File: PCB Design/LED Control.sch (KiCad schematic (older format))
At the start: 19 parts, among them J1 TO WS2812B LED STRIP, SW1 SW_Push_Dual

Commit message: circuit schematic complete
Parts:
- removed C1: 10uF, symbol Device:CP
- removed C1: 0.1nF, symbol Device:C
- added C1, C?: 0.1uF, symbol Device:C_Small
- added C?: C_Small, symbol Device:C_Small
- added C?: C, symbol Device:C
- added J?: Conn_01x03, symbol Connector_Generic:Conn_01x03
- added R?: R, symbol Device:R
- A1: symbol MCU_Module:Arduino_Nano_v3.x -> LED-Control-rescue:Arduino_Nano_v3.x-MCU_Module
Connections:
- net labels added: A3, DATA_IN, SS_DATA_OUT, SS_GND, SS_PWR, WS_GND, WS_PWR
- net labels removed: 5V_PWR, DATA, Earth
- wire segments 67 -> 93
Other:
- note added: "MICROCONTROLLER"
- note added: "POWER LINES"
- note added: "SOUND SENSOR"
- moved on the sheet: D1, D2, D3, J1, R1, R2, R3, R4, R5, R6, RV1, RV2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

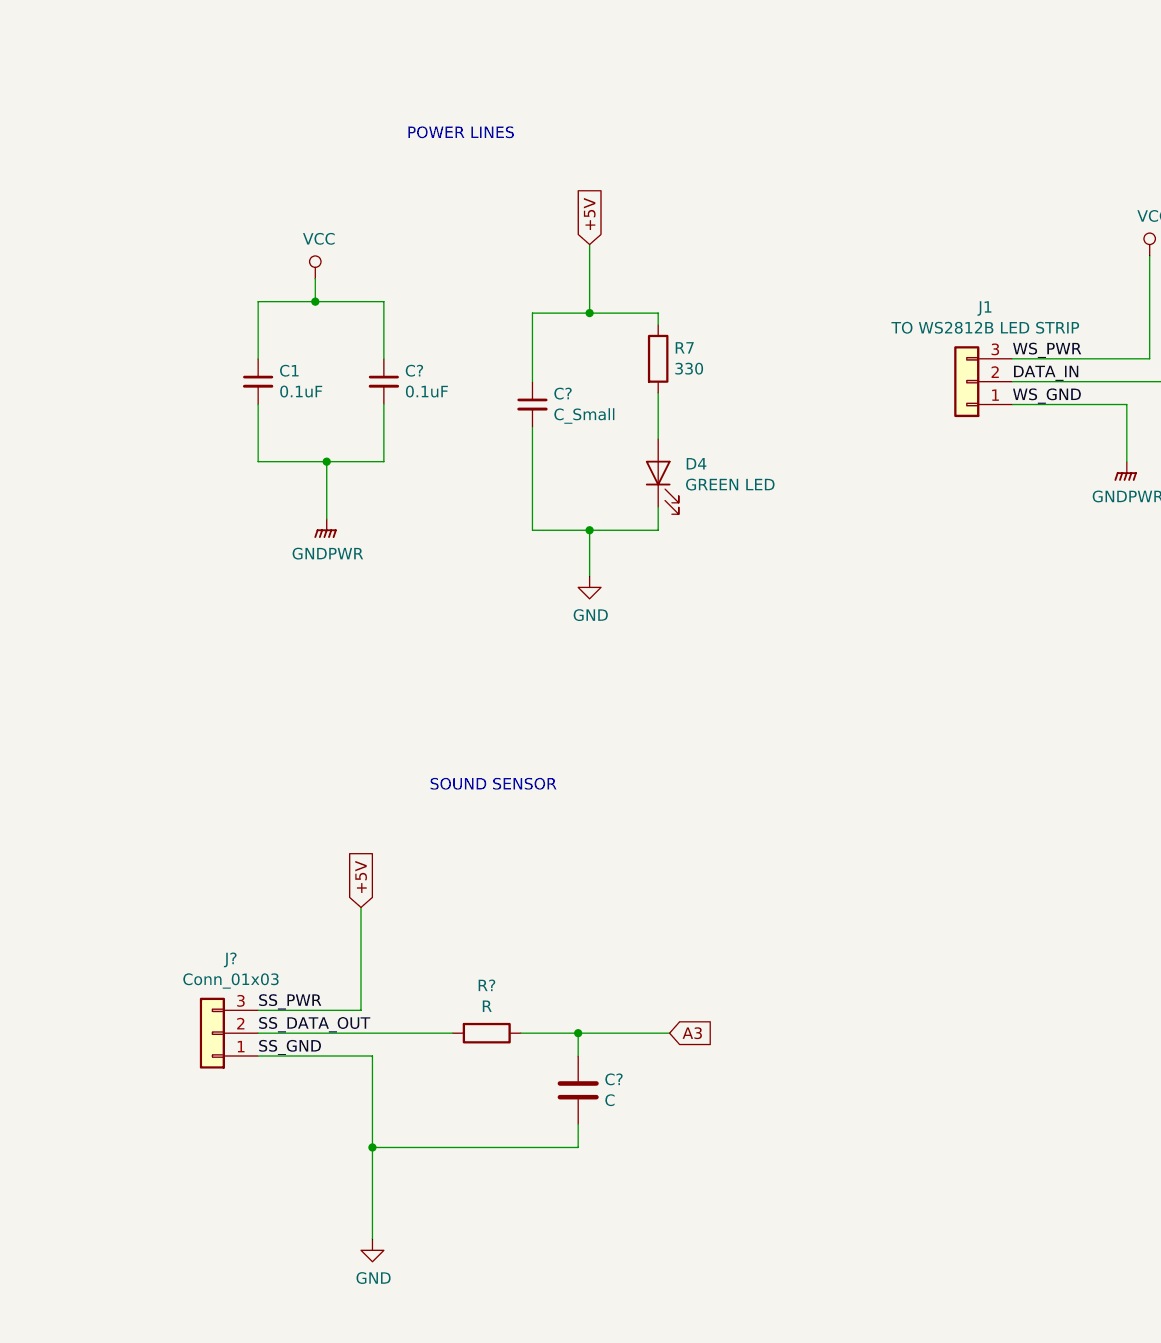
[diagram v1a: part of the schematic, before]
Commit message: PCB footprints added
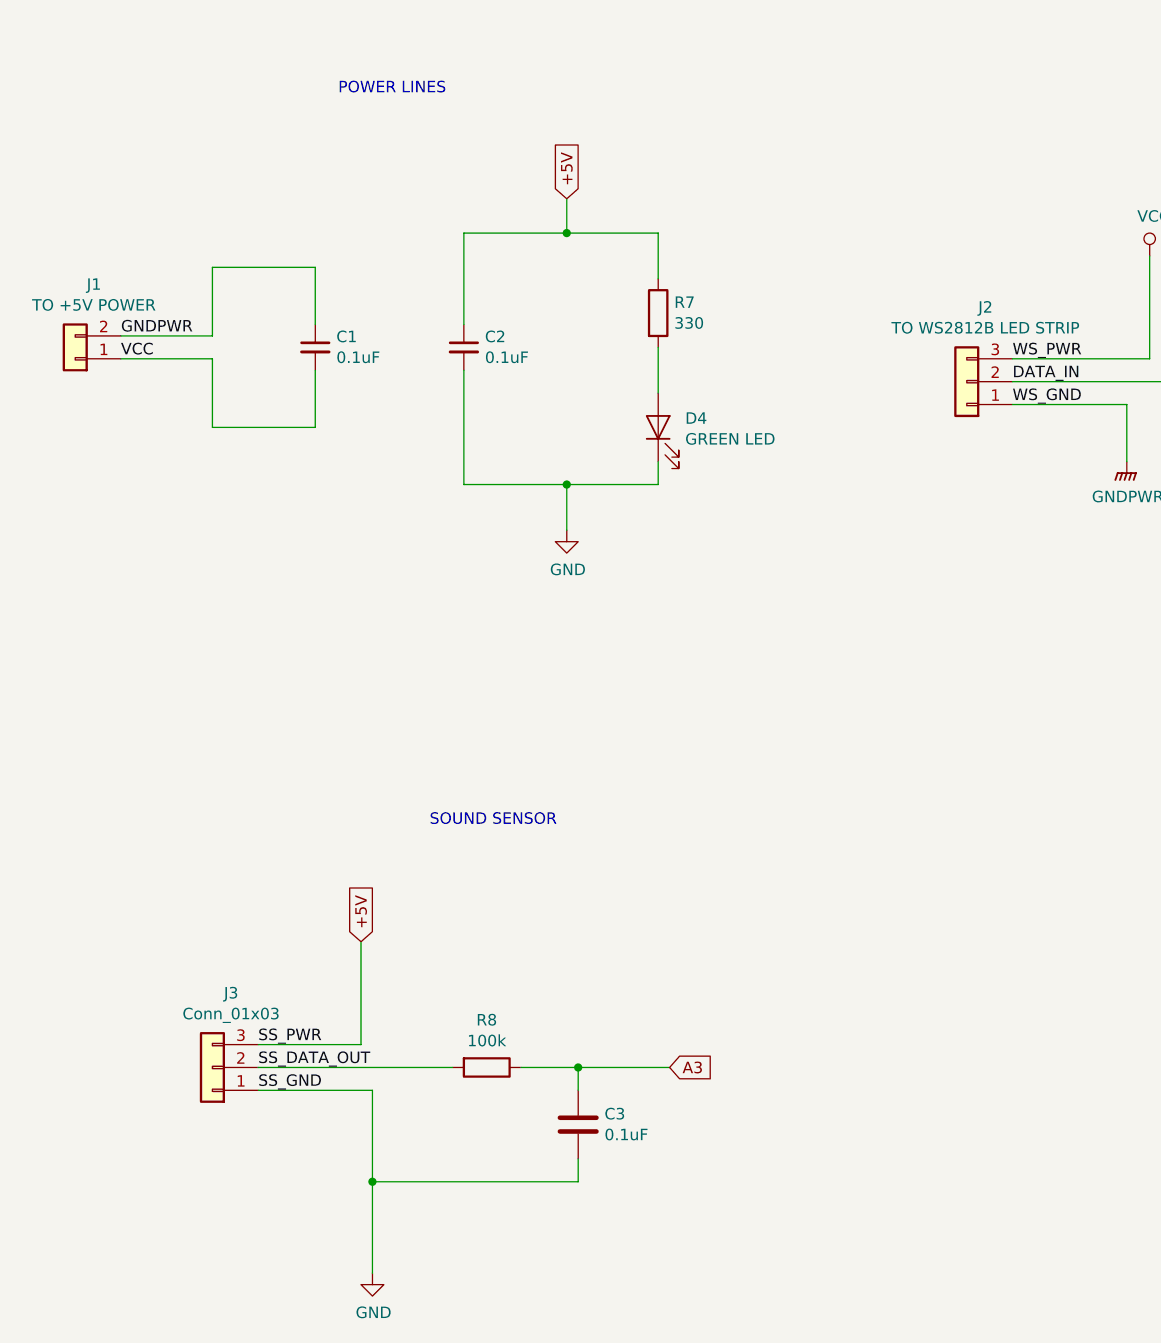
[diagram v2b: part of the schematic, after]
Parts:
- removed C?: C_Small, symbol Device:C_Small
- added J1: TO +5V POWER, TerminalBlock_Phoenix:TerminalBlock_Phoenix_PT-1,5-2-3.5-H_1x02_P3.50mm_Horizontal, symbol Connector_Generic:Conn_01x02
- C1: footprint (none) -> Capacitor_THT:C_Disc_D3.0mm_W1.6mm_P2.50mm
- C2: renamed from C?; footprint (none) -> Capacitor_THT:C_Disc_D3.0mm_W1.6mm_P2.50mm
- C3: renamed from C?; value C -> 0.1uF; footprint (none) -> Capacitor_THT:C_Disc_D3.0mm_W2.0mm_P2.50mm
- D1, D2, D3, D4: footprint (none) -> LED_THT:LED_D5.0mm
- J2: renamed from J1; footprint (none) -> TerminalBlock_Phoenix:TerminalBlock_Phoenix_MPT-0,5-3-2.54_1x03_P2.54mm_Horizontal
- J3: renamed from J?; footprint (none) -> TerminalBlock_Phoenix:TerminalBlock_Phoenix_MPT-0,5-3-2.54_1x03_P2.54mm_Horizontal
- R1, R2, R3, R4, R5, R6, R7: footprint (none) -> Resistor_THT:R_Axial_DIN0207_L6.3mm_D2.5mm_P10.16mm_Horizontal
- R8: renamed from R?; value R -> 100k; footprint (none) -> Resistor_THT:R_Axial_DIN0207_L6.3mm_D2.5mm_P10.16mm_Horizontal
- RV1, RV2, RV3: footprint (none) -> Custom Footprint:Potentiometer_4mm_Pitch
- SW1: footprint (none) -> Button_Switch_THT:SW_PUSH_6mm_H13mm
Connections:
- net +5V: now also C2.1
- net GND: now also C2.2
- net GNDPWR: now also C1.1, J1.2 (Pin_2); no longer C1.2, C2.2
- net VCC: now also C1.2, J1.1 (Pin_1); no longer C1.1, C2.1
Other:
- moved on the sheet: C1, C2, C3, D4, J3, R7, R8

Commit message: connectors selected and footprints updated
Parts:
- removed C3: 0.1uF, Capacitor_THT:C_Disc_D3.0mm_W2.0mm_P2.50mm, symbol Device:C
- removed J1: TO +5V POWER, TerminalBlock_Phoenix:TerminalBlock_Phoenix_PT-1,5-2-3.5-H_1x02_P3.50mm_Horizontal, symbol Connector_Generic:Conn_01x02
- added C2, C5: 0.1uF, Capacitor_THT:C_Disc_D3.0mm_W1.6mm_P2.50mm, symbol Device:C_Small
- added C4: 1uF, Capacitor_THT:C_Disc_D3.0mm_W1.6mm_P2.50mm, symbol Device:C_Small
- added J1: 5V 5A Power, PJ-002AH:CUI_PJ-002AH, symbol Connector:Barrel_Jack_Switch
- J2: footprint TerminalBlock_Phoenix:TerminalBlock_Phoenix_MPT-0,5-3-2.54_1x03_P2.54mm_Horizontal -> Connector_JST:JST_PH_S3B-PH-K_1x03_P2.00mm_Horizontal
- renumbered C2 to C3
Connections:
- net +5V: now also C4.1
- net A3: now also C5.1
- net GND: now also C4.2, C5.2
- net GNDPWR: now also C1.2, J2.3 (Pin_3), C2.2, J1.2; no longer C1.1, J2.1 (Pin_1)
- net VCC: now also C1.1, J2.1 (Pin_1), C2.1, J1.1; no longer C1.2, J2.3 (Pin_3)
- no-connect marks 2 -> 22
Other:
- moved on the sheet: A1, C1, C3, D1, D2, D3, D4, J2, J3, R1, R2, R3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

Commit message: capacitor footprints changed to axial
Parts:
- C1, C2, C3, C4, C5: footprint Capacitor_THT:C_Disc_D3.0mm_W1.6mm_P2.50mm -> Capacitor_THT:C_Axial_L3.8mm_D2.6mm_P7.50mm_Horizontal
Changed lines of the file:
@@
 F 0 "C1" H 3142 1996 50  0000 L CNN
 F 1 "0.1uF" H 3142 1905 50  0000 L CNN
-F 2 "Capacitor_THT:C_Disc_D3.0mm_W1.6mm_P2.50mm" H 3050 1950 50  0001 C CNN
+F 2 "Capacitor_THT:C_Axial_L3.8mm_D2.6mm_P7.50mm_Horizontal" H 3050 1950 50  0001 C CNN
 F 3 "~" H 3050 1950 50  0001 C CNN
 	1    3050 1950
@@
 F 0 "C3" H 2242 3646 50  0000 L CNN
 F 1 "0.1uF" H 2242 3555 50  0000 L CNN
-F 2 "Capacitor_THT:C_Disc_D3.0mm_W1.6mm_P2.50mm" H 2150 3600 50  0001 C CNN
+F 2 "Capacitor_THT:C_Axial_L3.8mm_D2.6mm_P7.50mm_Horizontal" H 2150 3600 50  0001 C CNN
 F 3 "~" H 2150 3600 50  0001 C CNN
 	1    2150 3600
@@
 F 0 "C2" H 3592 1996 50  0000 L CNN
 F 1 "0.1uF" H 3592 1905 50  0000 L CNN
-F 2 "Capacitor_THT:C_Disc_D3.0mm_W1.6mm_P2.50mm" H 3500 1950 50  0001 C CNN
+F 2 "Capacitor_THT:C_Axial_L3.8mm_D2.6mm_P7.50mm_Horizontal" H 3500 1950 50  0001 C CNN
 F 3 "~" H 3500 1950 50  0001 C CNN
 	1    3500 1950
@@
 F 0 "C4" H 2792 3646 50  0000 L CNN
 F 1 "1uF" H 2792 3555 50  0000 L CNN
-F 2 "Capacitor_THT:C_Disc_D3.0mm_W1.6mm_P2.50mm" H 2700 3600 50  0001 C CNN
+F 2 "Capacitor_THT:C_Axial_L3.8mm_D2.6mm_P7.50mm_Horizontal" H 2700 3600 50  0001 C CNN
 F 3 "~" H 2700 3600 50  0001 C CNN
 	1    2700 3600
@@
 F 0 "C5" H 3642 6496 50  0000 L CNN
 F 1 "0.1uF" H 3642 6405 50  0000 L CNN
-F 2 "Capacitor_THT:C_Disc_D3.0mm_W1.6mm_P2.50mm" H 3550 6450 50  0001 C CNN
+F 2 "Capacitor_THT:C_Axial_L3.8mm_D2.6mm_P7.50mm_Horizontal" H 3550 6450 50  0001 C CNN
 F 3 "~" H 3550 6450 50  0001 C CNN
 	1    3550 6450

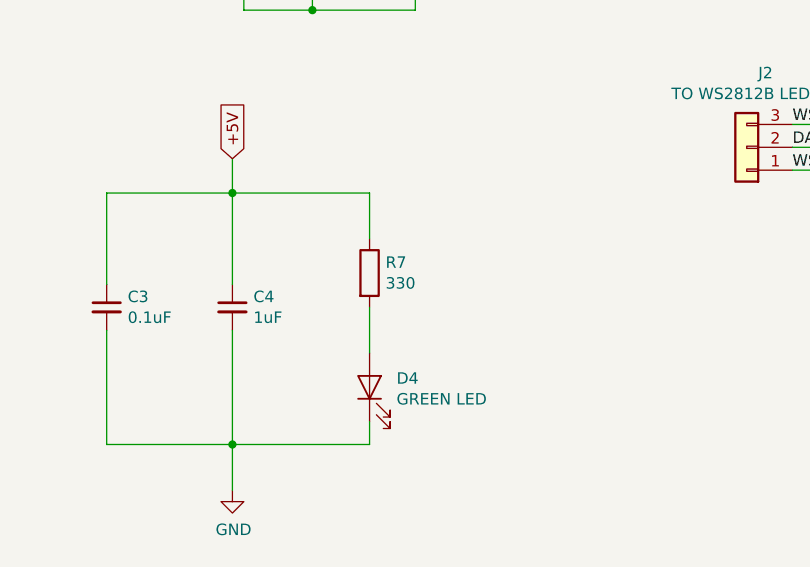
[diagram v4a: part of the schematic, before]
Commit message: Rs, Cs, LED updated for SMT
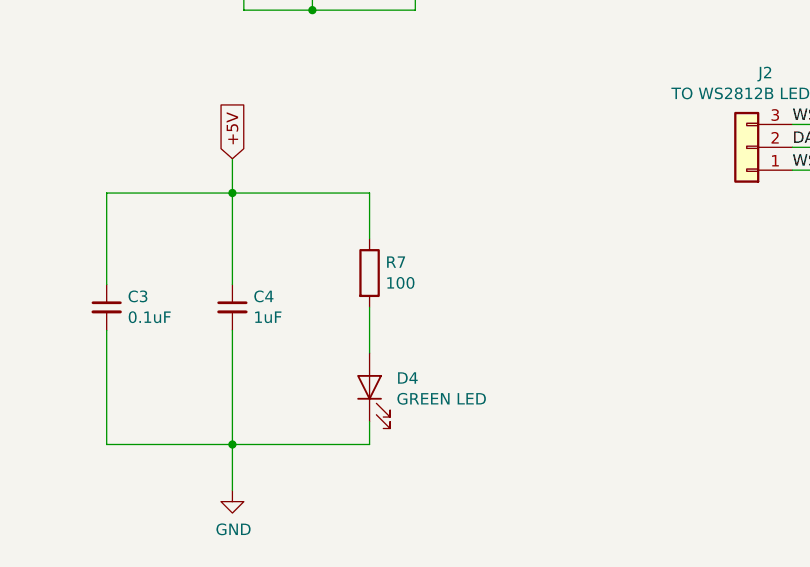
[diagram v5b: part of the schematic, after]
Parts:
- C1, C3: footprint Capacitor_THT:C_Axial_L3.8mm_D2.6mm_P7.50mm_Horizontal -> Capacitor_SMD:C_0603_1608Metric; LCSC (none) -> C14663
- C2, C4: footprint Capacitor_THT:C_Axial_L3.8mm_D2.6mm_P7.50mm_Horizontal -> Capacitor_SMD:C_0603_1608Metric; LCSC (none) -> C15849
- C5: footprint Capacitor_THT:C_Axial_L3.8mm_D2.6mm_P7.50mm_Horizontal -> Capacitor_THT:C_Disc_D3.4mm_W2.1mm_P2.50mm
- D4: footprint LED_THT:LED_D5.0mm -> LED_SMD:LED_0805_2012Metric; LCSC (none) -> C63855
- R1, R6: footprint Resistor_THT:R_Axial_DIN0207_L6.3mm_D2.5mm_P10.16mm_Horizontal -> Resistor_SMD:R_0805_2012Metric; LCSC (none) -> C17513
- R2, R3, R4, R5: footprint Resistor_THT:R_Axial_DIN0207_L6.3mm_D2.5mm_P10.16mm_Horizontal -> Resistor_SMD:R_0805_2012Metric; LCSC (none) -> C17630
- R7: value 330 -> 100; footprint Resistor_THT:R_Axial_DIN0207_L6.3mm_D2.5mm_P10.16mm_Horizontal -> Resistor_SMD:R_0805_2012Metric; LCSC (none) -> C17408
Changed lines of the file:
@@
 F 0 "R5" H 7420 4246 50  0000 L CNN
 F 1 "330" H 7420 4155 50  0000 L CNN
-F 2 "Resistor_THT:R_Axial_DIN0207_L6.3mm_D2.5mm_P10.16mm_Horizontal" V 7280 4200 50  0001 C CNN
+F 2 "Resistor_SMD:R_0805_2012Metric" V 7280 4200 50  0001 C CNN
 F 3 "~" H 7350 4200 50  0001 C CNN
+F 4 "C17630" H 7350 4200 50  0001 C CNN "LCSC"
 	1    7350 4200
 	1    0    0    -1
@@
 F 0 "R3" H 6120 4246 50  0000 L CNN
 F 1 "330" H 6120 4155 50  0000 L CNN
-F 2 "Resistor_THT:R_Axial_DIN0207_L6.3mm_D2.5mm_P10.16mm_Horizontal" V 5980 4200 50  0001 C CNN
+F 2 "Resistor_SMD:R_0805_2012Metric" V 5980 4200 50  0001 C CNN
 F 3 "~" H 6050 4200 50  0001 C CNN
+F 4 "C17630" H 6050 4200 50  0001 C CNN "LCSC"
 	1    6050 4200
 	1    0    0    -1
@@
 F 0 "R4" H 6770 4246 50  0000 L CNN
 F 1 "330" H 6770 4155 50  0000 L CNN
-F 2 "Resistor_THT:R_Axial_DIN0207_L6.3mm_D2.5mm_P10.16mm_Horizontal" V 6630 4200 50  0001 C CNN
+F 2 "Resistor_SMD:R_0805_2012Metric" V 6630 4200 50  0001 C CNN
 F 3 "~" H 6700 4200 50  0001 C CNN
+F 4 "C17630" H 6700 4200 50  0001 C CNN "LCSC"
 	1    6700 4200
 	1    0    0    -1
@@
 F 0 "R1" H 7620 2546 50  0000 L CNN
 F 1 "1k" H 7620 2455 50  0000 L CNN
-F 2 "Resistor_THT:R_Axial_DIN0207_L6.3mm_D2.5mm_P10.16mm_Horizontal" V 7480 2500 50  0001 C CNN
+F 2 "Resistor_SMD:R_0805_2012Metric" V 7480 2500 50  0001 C CNN
 F 3 "~" H 7550 2500 50  0001 C CNN
+F 4 "C17513" H 7550 2500 50  0001 C CNN "LCSC"
 	1    7550 2500
 	1    0    0    -1
@@
 F 0 "R6" V 9157 5000 50  0000 C CNN
 F 1 "1k" V 9066 5000 50  0000 C CNN
-F 2 "Resistor_THT:R_Axial_DIN0207_L6.3mm_D2.5mm_P10.16mm_Horizontal" V 8880 5000 50  0001 C CNN
+F 2 "Resistor_SMD:R_0805_2012Metric" V 8880 5000 50  0001 C CNN
 F 3 "~" H 8950 5000 50  0001 C CNN
+F 4 "C17513" V 8950 5000 50  0001 C CNN "LCSC"
 	1    8950 5000
 	0    -1   -1   0
@@
 F 0 "R2" V 6543 3350 50  0000 C CNN
 F 1 "330" V 6634 3350 50  0000 C CNN
-F 2 "Resistor_THT:R_Axial_DIN0207_L6.3mm_D2.5mm_P10.16mm_Horizontal" V 6680 3350 50  0001 C CNN
+F 2 "Resistor_SMD:R_0805_2012Metric" V 6680 3350 50  0001 C CNN
 F 3 "~" H 6750 3350 50  0001 C CNN
+F 4 "C17630" V 6750 3350 50  0001 C CNN "LCSC"
 	1    6750 3350
 	0    1    1    0
@@
 P 3300 3450
 F 0 "R7" H 3370 3496 50  0000 L CNN
-F 1 "330" H 3370 3405 50  0000 L CNN
-F 2 "Resistor_THT:R_Axial_DIN0207_L6.3mm_D2.5mm_P10.16mm_Horizontal" V 3230 3450 50  0001 C CNN
+F 1 "100" H 3370 3405 50  0000 L CNN
+F 2 "Resistor_SMD:R_0805_2012Metric" V 3230 3450 50  0001 C CNN
 F 3 "~" H 3300 3450 50  0001 C CNN
+F 4 "C17408" H 3300 3450 50  0001 C CNN "LCSC"
 	1    3300 3450
 	1    0    0    -1
@@
 F 0 "D4" V 3339 3832 50  0000 R CNN
 F 1 "GREEN LED" V 3248 3832 50  0000 R CNN
-F 2 "LED_THT:LED_D5.0mm" H 3300 3950 50  0001 C CNN
+F 2 "LED_SMD:LED_0805_2012Metric" H 3300 3950 50  0001 C CNN
 F 3 "~" H 3300 3950 50  0001 C CNN
+F 4 "C63855" V 3300 3950 50  0001 C CNN "LCSC"
 	1    3300 3950
 	0    -1   -1   0
@@
 +5V
 $Comp
-L Device:C_Small C1
-U 1 1 5E34619E
-P 3050 1950
-F 0 "C1" H 3142 1996 50  0000 L CNN
-F 1 "0.1uF" H 3142 1905 50  0000 L CNN
-F 2 "Capacitor_THT:C_Axial_L3.8mm_D2.6mm_P7.50mm_Horizontal" H 3050 1950 50  0001 C CNN
-F 3 "~" H 3050 1950 50  0001 C CNN
-	1    3050 1950
-	1    0    0    -1
-$EndComp
-$Comp
 L Device:C_Small C3
 U 1 1 5E347A50
@@
 F 0 "C3" H 2242 3646 50  0000 L CNN
 F 1 "0.1uF" H 2242 3555 50  0000 L CNN
-F 2 "Capacitor_THT:C_Axial_L3.8mm_D2.6mm_P7.50mm_Horizontal" H 2150 3600 50  0001 C CNN
+F 2 "Capacitor_SMD:C_0603_1608Metric" H 2150 3600 50  0001 C CNN
 F 3 "~" H 2150 3600 50  0001 C CNN
+F 4 "C14663" H 2150 3600 50  0001 C CNN "LCSC"
 	1    2150 3600
 	1    0    0    -1
@@
 F 0 "C2" H 3592 1996 50  0000 L CNN
 F 1 "0.1uF" H 3592 1905 50  0000 L CNN
-F 2 "Capacitor_THT:C_Axial_L3.8mm_D2.6mm_P7.50mm_Horizontal" H 3500 1950 50  0001 C CNN
+F 2 "Capacitor_SMD:C_0603_1608Metric" H 3500 1950 50  0001 C CNN
 F 3 "~" H 3500 1950 50  0001 C CNN
+F 4 "C15849" H 3500 1950 50  0001 C CNN "LCSC"
 	1    3500 1950
 	1    0    0    -1
@@
 F 0 "C4" H 2792 3646 50  0000 L CNN
 F 1 "1uF" H 2792 3555 50  0000 L CNN
-F 2 "Capacitor_THT:C_Axial_L3.8mm_D2.6mm_P7.50mm_Horizontal" H 2700 3600 50  0001 C CNN
+F 2 "Capacitor_SMD:C_0603_1608Metric" H 2700 3600 50  0001 C CNN
 F 3 "~" H 2700 3600 50  0001 C CNN
+F 4 "C15849" H 2700 3600 50  0001 C CNN "LCSC"
 	1    2700 3600
 	1    0    0    -1
@@
 F 0 "C5" H 3642 6496 50  0000 L CNN
 F 1 "0.1uF" H 3642 6405 50  0000 L CNN
-F 2 "Capacitor_THT:C_Axial_L3.8mm_D2.6mm_P7.50mm_Horizontal" H 3550 6450 50  0001 C CNN
+F 2 "Capacitor_THT:C_Disc_D3.4mm_W2.1mm_P2.50mm" H 3550 6450 50  0001 C CNN
 F 3 "~" H 3550 6450 50  0001 C CNN
 	1    3550 6450
@@
 Wire Wire Line
 	3550 6550 3550 6750
+$Comp
+L Device:C_Small C1
+U 1 1 5E34619E
+P 3050 1950
+F 0 "C1" H 3142 1996 50  0000 L CNN
+F 1 "0.1uF" H 3142 1905 50  0000 L CNN
+F 2 "Capacitor_SMD:C_0603_1608Metric" H 3050 1950 50  0001 C CNN
+F 3 "~" H 3050 1950 50  0001 C CNN
+F 4 "C14663" H 3050 1950 50  0001 C CNN "LCSC"
+	1    3050 1950
+	1    0    0    -1
+$EndComp
 $EndSCHEMATC
